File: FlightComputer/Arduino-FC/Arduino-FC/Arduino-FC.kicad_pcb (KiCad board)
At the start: 2 copper layers, 128.5 x 95.7 mm, 26 parts, among them J1 Conn_01x04, J2 Conn_01x08, J3 Conn_01x06, J4 Conn_01x03, J5 Screw_Terminal_01x02, J6 Conn_01x02, J7 Conn_01x02, U1 NRF24L01_Breakout

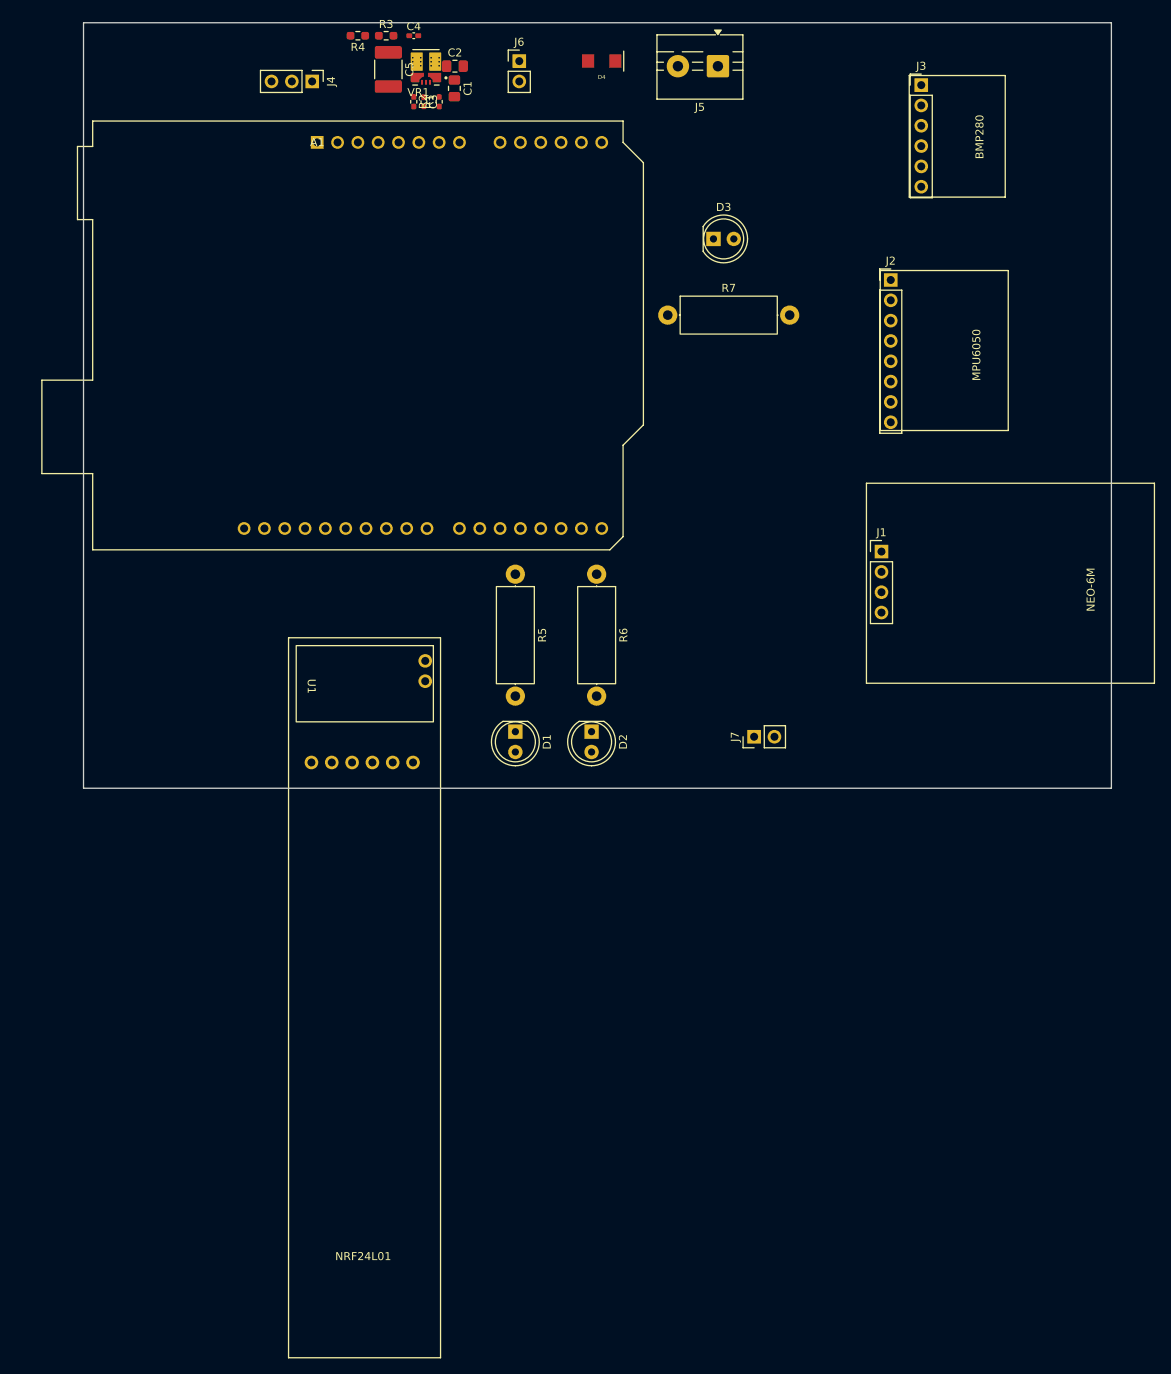
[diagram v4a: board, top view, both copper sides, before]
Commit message: Mounting Holes Added
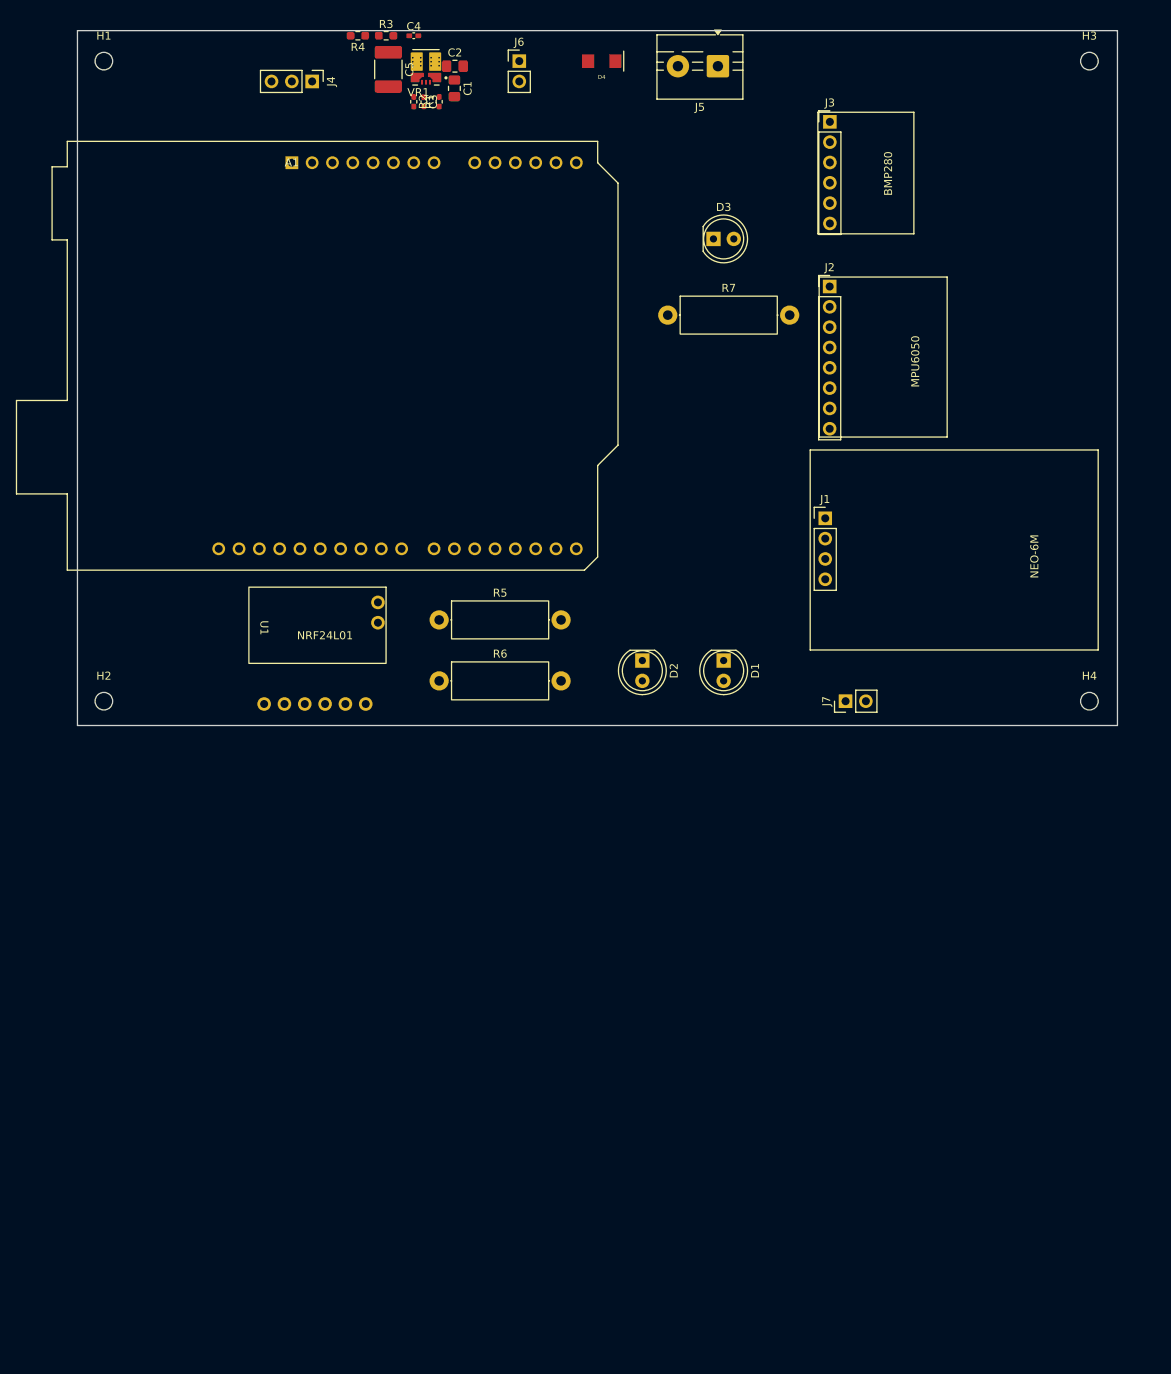
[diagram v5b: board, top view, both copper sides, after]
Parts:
- added H1: MountingHole, MountingHole:MountingHole_2.2mm_M2, F.Cu at (95.2, 47.0)
- added H2: MountingHole, MountingHole:MountingHole_2.2mm_M2, F.Cu at (95.2, 127.0)
- added H3: MountingHole, MountingHole:MountingHole_2.2mm_M2, F.Cu at (218.4, 47.0)
- added H4: MountingHole, MountingHole:MountingHole_2.2mm_M2, F.Cu at (218.4, 127.0)
- moved D1 27.5 mm to (172.7, 121.9)
- moved R6 23.8 mm to (137.2, 124.5), turned to 0 degrees
- moved J3 12.3 mm to (186.0, 54.6)
- moved J7 12.3 mm to (188.0, 127.0)
- moved R5 11.1 mm to (137.2, 116.8), turned to 0 degrees
- moved D2 10.9 mm to (162.6, 121.9)
- moved U1 9.40 mm to (121.6, 124.8)
- moved J1 8.17 mm to (185.4, 104.1)
- moved J2 7.68 mm to (186.0, 75.2)
- moved A1 4.07 mm to (118.7, 59.7)
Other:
- board size 128.5 x 95.7 mm -> 130 x 86.9 mm

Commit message: Design Constraints
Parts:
- moved J5 45.0 mm to (127.0, 48.3)
- moved J4 44.0 mm to (165.1, 53.3)
- moved D4 24.3 mm to (133.3, 49.5), turned to 90 degrees
- moved D3 19.5 mm to (177.8, 50.8), turned to 90 degrees
- moved H2 17.8 mm to (113.0, 125.7)
- moved H4 17.8 mm to (200.7, 125.7)
- moved H1 17.8 mm to (113.0, 47.0)
- moved H3 17.8 mm to (200.7, 47.0)
- moved J6 16.9 mm to (132.1, 54.6), turned to 90 degrees
- moved R7 14.3 mm to (177.8, 71.1), turned to 90 degrees
- moved A1 13.3 mm to (132.1, 59.7)
- moved C2 13.3 mm to (152.4, 48.3)
- moved C1 12.2 mm to (151.1, 52.3)
- moved C3 12.2 mm to (147.3, 54.0)
- moved C4 12.2 mm to (146.1, 45.7)
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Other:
- board size 130 x 86.9 mm -> 95 x 86.9 mm

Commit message: Major Layout + Logo
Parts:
- added G***: LOGO, Logo:Logo, F.Cu at (178.3, 83.6)
- moved R6 17.0 mm to (155.4, 115.5), turned to 180 degrees
- moved R5 16.6 mm to (155.4, 125.1), turned to 180 degrees
- moved R7 15.3 mm to (177.8, 55.9), turned to -90 degrees
- moved D1 12.8 mm to (169.0, 126.5), turned to 90 degrees
- moved R4 12.6 mm to (151.6, 47.2)
- moved C1 12.5 mm to (138.9, 49.4), turned to 90 degrees
- moved C2 11.3 mm to (141.2, 49.4), turned to 90 degrees
- moved R3 10.8 mm to (152.6, 50.0), turned to 90 degrees
- moved D2 8.42 mm to (169.0, 117.0), turned to 90 degrees
- moved J6 7.17 mm to (133.3, 47.5)
- moved R1 6.91 mm to (143.4, 50.2), turned to 180 degrees
- moved C3 6.88 mm to (147.6, 47.1), turned to 0 degrees
- moved R2 5.95 mm to (143.4, 48.6), turned to 180 degrees
- moved C5 5.56 mm to (145.7, 54.8), turned to 180 degrees
- moved J4 5.35 mm to (162.8, 48.5), turned to 0 degrees
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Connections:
- A1 pad 2: unconnected-(A1-IOREF-Pad2) -> +5V
- C4 pad 1: Net-(VR1-VOUT) -> +5V
- C5 pad 1: Net-(VR1-VOUT) -> +5V
- R3 pad 1: Net-(VR1-VOUT) -> +5V
- VR1 pad 3: Net-(VR1-VOUT) -> +5V
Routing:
- net +3V3: track 0.00 -> 159.9 mm
- net +5V: track 0.00 -> 139.0 mm
- net /BMP_SDA: track 0.00 -> 60.3 mm
- net /BMP_SCL: track 0.00 -> 49.4 mm, vias 0 -> 2
- net /NRF_CE: track 0.00 -> 42.2 mm, vias 0 -> 2
- net /NRF_CSN: track 0.00 -> 36.9 mm, vias 0 -> 2
- net /NRF_MOSI: track 0.00 -> 32.7 mm, vias 0 -> 2
- net Net-(A1-D6): track 0.00 -> 28.8 mm
- net /NRF_SCK: track 0.00 -> 27.7 mm
- net /NRF_MISO: track 0.00 -> 24.0 mm
- net /GPS_TX: track 0.00 -> 19.7 mm
- net /GPS_RX: track 0.00 -> 16.8 mm
- net Net-(A1-D5): track 0.00 -> 16.8 mm
- net Net-(D2-K): track 0.00 -> 14.2 mm
- net Net-(D1-K): track 0.00 -> 14.2 mm
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- added copper zone on B.Cu, net GND
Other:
- board text added: "(symbol "LOGO" (pin_names (offset 1.016)) (in_bom yes) (on_board yes) (property "Reference" "#G" (at 0 3.36525 0) (effects (font (size 1.27 1.27)) hide) ) (property "Value" "LOGO" (at 0 -3.36525 0) (effects (font (size 1.27 1.27)) hide) ) (property "Footprint" "" (at 0 0 0) (effects (font (size 1.27 1.27)) hide) ) (property "Datasheet" "" (at 0 0 0) (effects (font (size 1.27 1.27)) hide) ) (symbo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"
- board text added: "+"
- board text added: "ARM"
- board text added: "POWER"
- board text added: "SAFE"
- board text added: "SERVO"
- board text added: "SWITCH"

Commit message: Background Slikscreen
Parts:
- added G***: LOGO, Logo:litework_logo, F.Cu at (189.0, 126.5)
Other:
- board text added: "Designed By: Fawaaz Kamali Siddiqui"
- board text added: "GitHub: https://github.com/fawaaz-kamali/CANSAT-LiteWork-2026"
- board text added: "STEC Initiative 2026 (TMU CanSat) Team 'lite Work Fawaaz Kamali Siddiqui Hamid Karimi Mohammad Alwattar Ben Reboks Basim Allawala"
